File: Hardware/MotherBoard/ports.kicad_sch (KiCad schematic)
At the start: 7 parts, among them J10 USR_DATA, J14 PORT1, J16 PORT2, J17 PORT2, J18 PORT3, J24 USR_CTRL, J5 USR_ADDR

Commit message: Finalize 1.3
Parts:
- J17: value PORT2 -> PORT3
- J18: value PORT3 -> PORT4/ROM
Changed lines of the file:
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@@
   (title_block
     (title "Miniish")
-    (date "2020-10-10")
+    (date "2023-05-19")
     (rev "v1.3")
     (company "Romuald Rousseau")
@@
       (effects (font (size 1.27 1.27)))
     )
-    (property "Value" "PORT2" (at 172.72 31.75 0)
+    (property "Value" "PORT3" (at 172.72 31.75 0)
       (effects (font (size 1.27 1.27)))
     )
@@
       (effects (font (size 1.27 1.27)))
     )
-    (property "Value" "PORT3" (at 228.6 31.75 0)
-      (effects (font (size 1.27 1.27)))
-    )
+    (property "Value" "PORT4/ROM" (at 228.6 31.75 0)
+      (effects (font (size 1.27 1.27)))
+    )

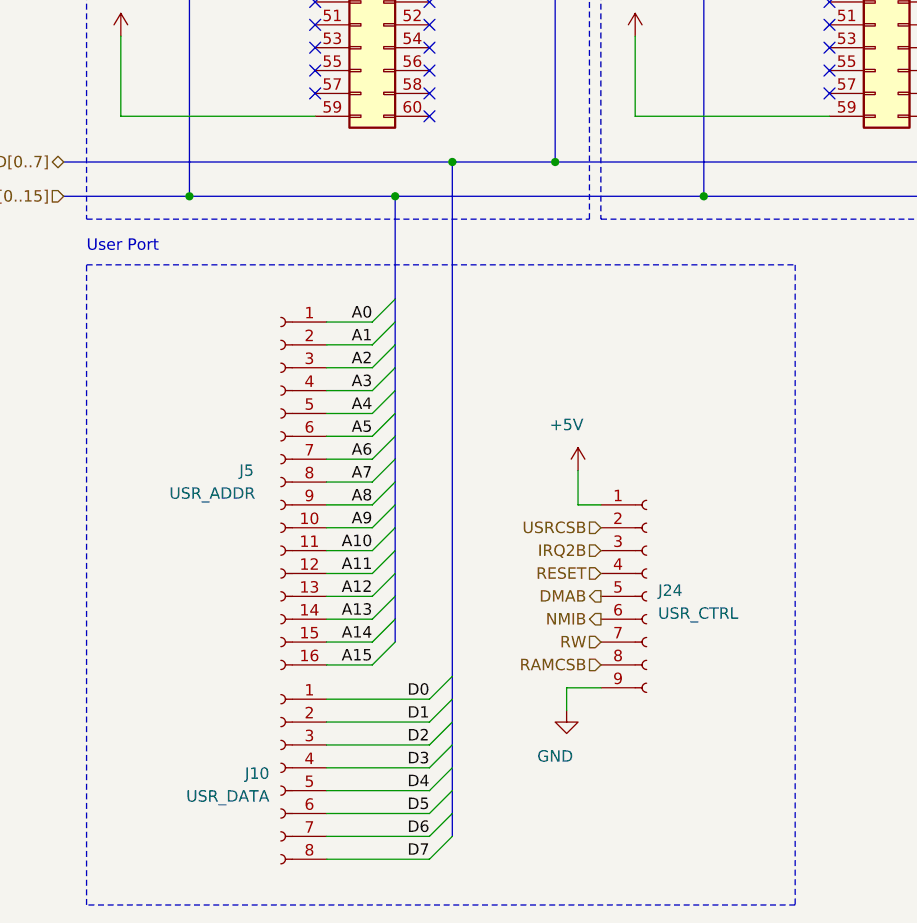
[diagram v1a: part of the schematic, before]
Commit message: Add SPI Board
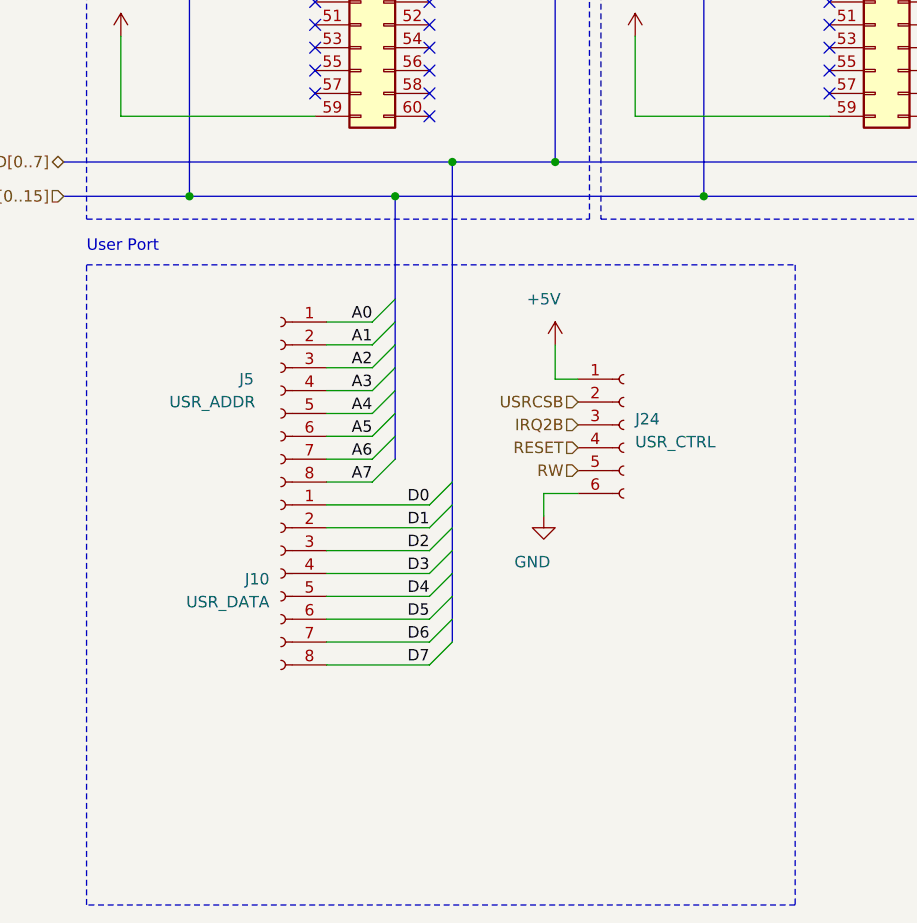
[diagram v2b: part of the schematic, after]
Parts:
- J24: footprint Connector_PinHeader_2.54mm:PinHeader_1x09_P2.54mm_Vertical -> Connector_PinHeader_2.54mm:PinHeader_2x03_P2.54mm_Vertical; symbol Connector:Conn_01x09_Socket -> Connector:Conn_01x06_Socket
- J5: footprint Connector_PinHeader_2.54mm:PinHeader_1x16_P2.54mm_Vertical -> Connector_PinHeader_2.54mm:PinHeader_1x08_P2.54mm_Vertical; symbol Connector:Conn_01x16_Socket -> Connector:Conn_01x08_Socket
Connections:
- net A10: no longer J5.11 (Pin_11)
- net A11: no longer J5.12 (Pin_12)
- net A12: no longer J5.13 (Pin_13)
- net A13: no longer J5.14 (Pin_14)
- net A14: no longer J5.15 (Pin_15)
- net A15: no longer J5.16 (Pin_16)
- net A8: no longer J5.9 (Pin_9)
- net A9: no longer J5.10 (Pin_10)
- net DMAB: no longer J24.5 (Pin_5)
- net GND: now also J24.6 (Pin_6); no longer J24.9 (Pin_9)
- net NMIB: no longer J24.6 (Pin_6)
- net RAMCSB: no longer J24.8 (Pin_8)
- net RW: now also J24.5 (Pin_5); no longer J24.7 (Pin_7)
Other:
- moved on the sheet: J10

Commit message: A lot of new hardware
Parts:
- J14, J16, J17, J18: footprint NESConnector:NES_Cartdrige -> Connector_NES:NES_Cartdrige
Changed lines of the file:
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@@
       (effects (font (size 1.27 1.27)))
     )
-    (property "Footprint" "NESConnector:NES_Cartdrige" (at 114.3 69.85 0)
+    (property "Footprint" "Connector_NES:NES_Cartdrige" (at 114.3 69.85 0)
       (effects (font (size 1.27 1.27)) hide)
     )
@@
       (effects (font (size 1.27 1.27)))
     )
-    (property "Footprint" "NESConnector:NES_Cartdrige" (at 171.45 69.85 0)
+    (property "Footprint" "Connector_NES:NES_Cartdrige" (at 171.45 69.85 0)
       (effects (font (size 1.27 1.27)) hide)
     )
@@
       (effects (font (size 1.27 1.27)))
     )
-    (property "Footprint" "NESConnector:NES_Cartdrige" (at 57.15 69.85 0)
+    (property "Footprint" "Connector_NES:NES_Cartdrige" (at 57.15 69.85 0)
       (effects (font (size 1.27 1.27)) hide)
     )
@@
       (effects (font (size 1.27 1.27)) hide)
     )
+    (property "Sim.Enable" "0" (at 48.26 158.75 0)
+      (effects (font (size 1.27 1.27)) hide)
+    )
     (pin "1")
     (pin "2")
@@
       (effects (font (size 1.27 1.27)) hide)
     )
+    (property "Sim.Enable" "0" (at 48.26 138.43 0)
+      (effects (font (size 1.27 1.27)) hide)
+    )
     (pin "1")
     (pin "2")
@@
       (effects (font (size 1.27 1.27)))
     )
-    (property "Footprint" "NESConnector:NES_Cartdrige" (at 227.33 69.85 0)
-      (effects (font (size 1.27 1.27)) hide)
-    )
+    (property "Footprint" "Connector_NES:NES_Cartdrige" (at 227.33 69.85 0)
+      (effects (font (size 1.27 1.27)) hide)
+    )

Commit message: Add ArduinoMultiInterface
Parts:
- renumbered J5 to J12, J10 to J13, J24 to J15
